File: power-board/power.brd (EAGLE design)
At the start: 100 x 80 mm, 2 parts, among them IC1 7805TV

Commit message: pow
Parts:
- added C1, C2, C3, C4: 100 nF, resistor:C025-025X050
- added D1: (no value), SparkFun-LED:LED5MM
- added R1: 470, resistor:0207/10
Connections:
- new net N$1: IC1.1, JP1.GND, R1.1
- new net N$2: D1.K, IC1.2, JP1.PWR
- new net N$3: D1.A, R1.2
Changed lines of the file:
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@@
 </element>
 <element name="IC1" library="linear" package="TO220V" value="7805TV" x="6.35" y="0"/>
+<element name="D1" library="SparkFun-LED" package="LED5MM" value="" x="3.81" y="-11.43"/>
+<element name="R1" library="resistor" package="0207/10" value="470" x="6.35" y="-19.05"/>
+<element name="C1" library="resistor" package="C025-025X050" value="100 nF" x="3.81" y="-24.13"/>
+<element name="C2" library="resistor" package="C025-025X050" value="100 nF" x="3.81" y="-31.75"/>
+<element name="C3" library="resistor" package="C025-025X050" value="100 nF" x="3.81" y="-39.37"/>
+<element name="C4" library="resistor" package="C025-025X050" value="100 nF" x="3.81" y="-46.99"/>
 </elements>
 <signals>
+<signal name="N$1">
+<contactref element="JP1" pad="GND"/>
+<contactref element="IC1" pad="1"/>
+<contactref element="R1" pad="1"/>
+<wire x1="3.81" y1="-2.54" x2="11.4554" y2="35.767" width="0" layer="19" extent="1-1"/>
+<wire x1="1.27" y1="-19.05" x2="3.81" y2="-2.54" width="0" layer="19" extent="1-1"/>
+</signal>
+<signal name="N$2">
+<contactref element="JP1" pad="PWR"/>
+<contactref element="IC1" pad="2"/>
+<contactref element="D1" pad="K"/>
+<wire x1="6.35" y1="-2.54" x2="11.43" y2="43.0878" width="0" layer="19" extent="1-1"/>
+<wire x1="5.08" y1="-11.43" x2="6.35" y2="-2.54" width="0" layer="19" extent="1-1"/>
+</signal>
+<signal name="N$3">
+<contactref element="R1" pad="2"/>
+<contactref element="D1" pad="A"/>
+<wire x1="2.54" y1="-11.43" x2="11.43" y2="-19.05" width="0" layer="19" extent="1-1"/>
+</signal>
 </signals>
 </board>

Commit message: power board ok
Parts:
- removed C3, C4: 100 nF, resistor:C025-025X050
- added ARDU: (no value), pinhead:1X03
- added DISPLAY, LED: (no value), pinhead:1X02
- added FOTOC: (no value), pinhead:1X04
- C2: value 100 nF -> 330 nF
- JP1: value POWER_JACKPTH_LOCK -> POWER_JACKPTH; device SparkFun-Connectors:POWER_JACK_PTH_LOCK -> SparkFun-Connectors:POWER_JACK_PTH
- R1: value 470 -> 680
- moved C1 55.9 mm to (3.81, 31.8), turned to 270 degrees
- moved C2 55.9 mm to (3.81, 24.1), turned to 270 degrees
- moved IC1 28.0 mm to (7.62, 27.9), turned to 90 degrees
- moved JP1 21.6 mm to (-5.08, 15.2), turned to 270 degrees
- moved D1 21.0 mm to (12.7, 7.62), turned to 270 degrees
- moved R1 20.3 mm to (6.35, 1.27)
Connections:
- removed net N$3: D1.A, R1.2
- new net N$5: ARDU.3, C1.2, C2.1, DISPLAY.2, FOTOC.3, FOTOC.4, IC1.2, JP1.GND, LED.2, R1.1
- new net N$6: C1.1, DISPLAY.1, IC1.3, LED.1
- net N$1: now also D1.K, R1.2; no longer IC1.1, JP1.GND, R1.1
- net N$2: now also ARDU.1, C2.2, D1.A, FOTOC.1, FOTOC.2, IC1.1; no longer D1.K, IC1.2
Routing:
- net N$5: track 0.00 -> 101.4 mm
- net N$2: track 0.00 -> 45.0 mm
- net N$6: track 0.00 -> 29.6 mm
- net N$3: track 0.00 -> 23.4 mm
- net N$1: track 0.00 -> 5.24 mm
- added copper zone on layer 16, net GND
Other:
- board size 100 x 80 mm -> 26.3 x 45.7 mm

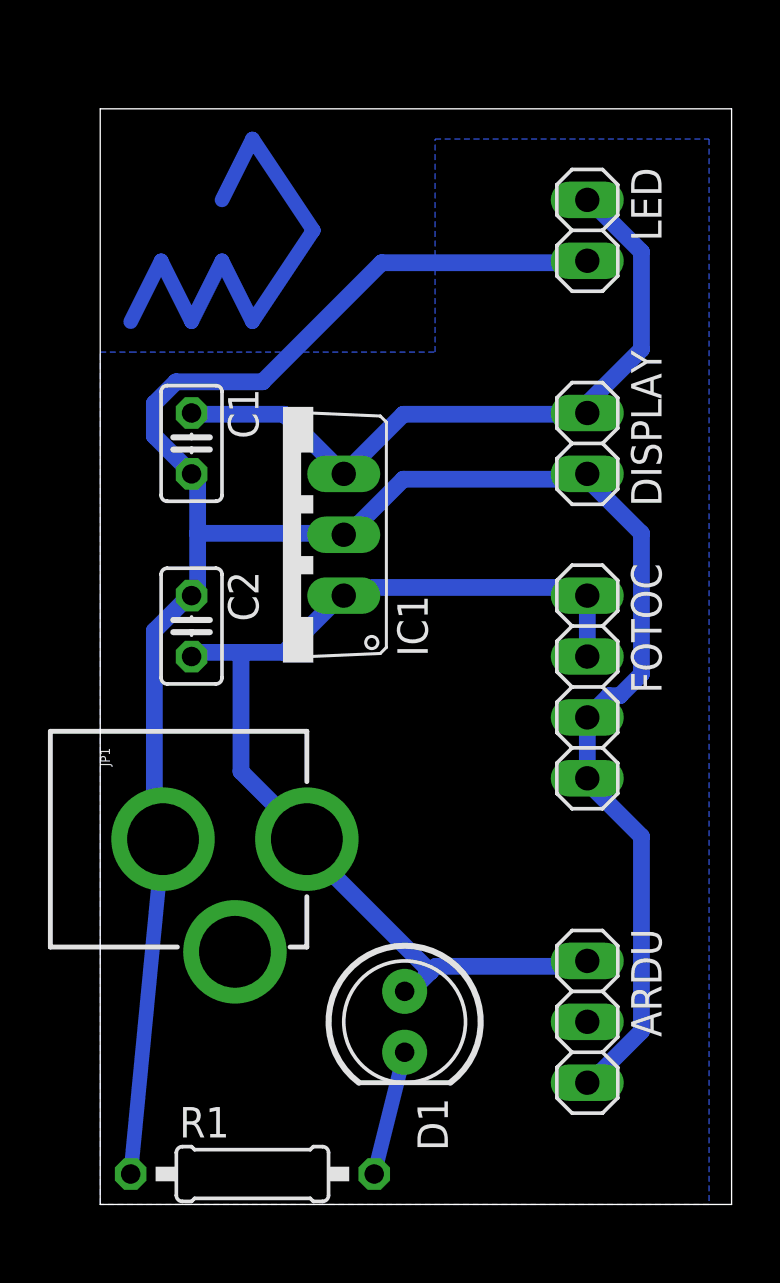
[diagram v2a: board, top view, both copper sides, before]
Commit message: Power board printed
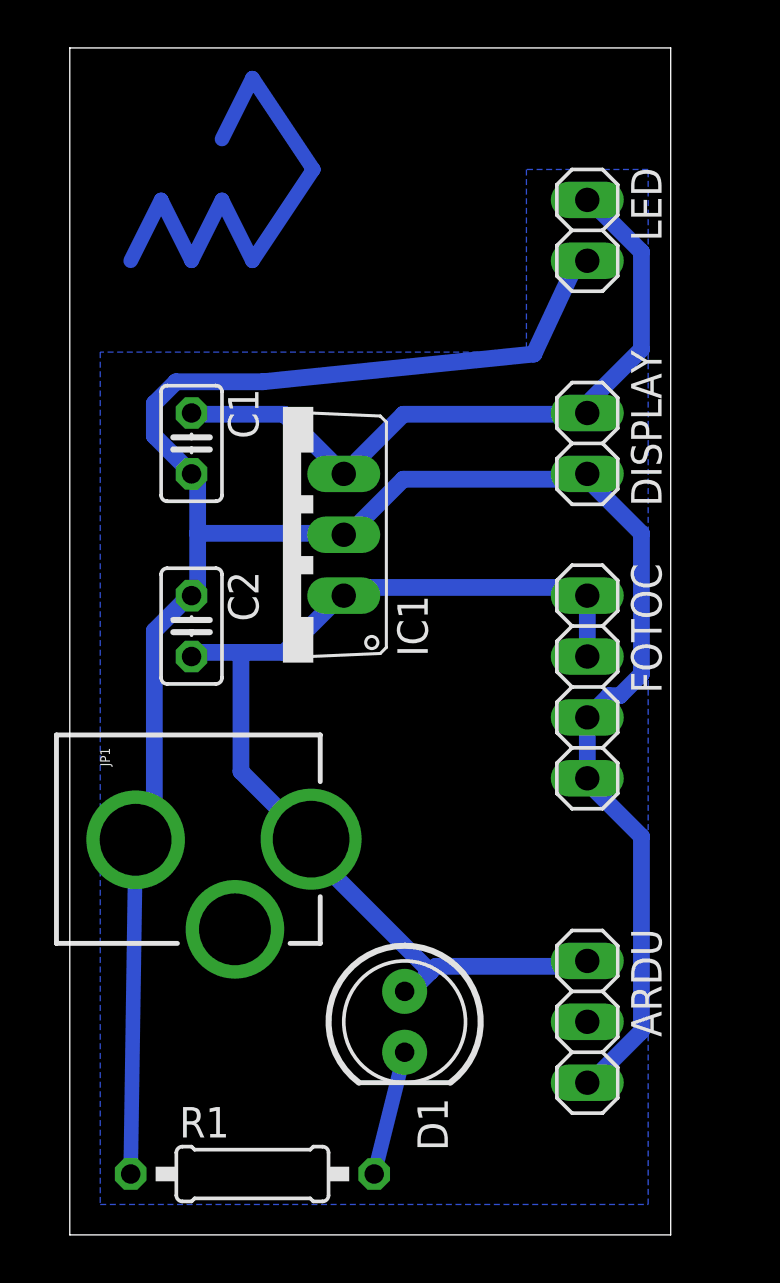
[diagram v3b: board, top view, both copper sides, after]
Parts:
- JP1: value POWER_JACKPTH -> POWER_JACKPTH_LOCK; device SparkFun-Connectors:POWER_JACK_PTH -> SparkFun-Connectors:POWER_JACK_PTH_LOCK
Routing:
- net N$5: track 101.4 -> 102.2 mm
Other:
- board size 26.3 x 45.7 mm -> 25.1 x 49.5 mm

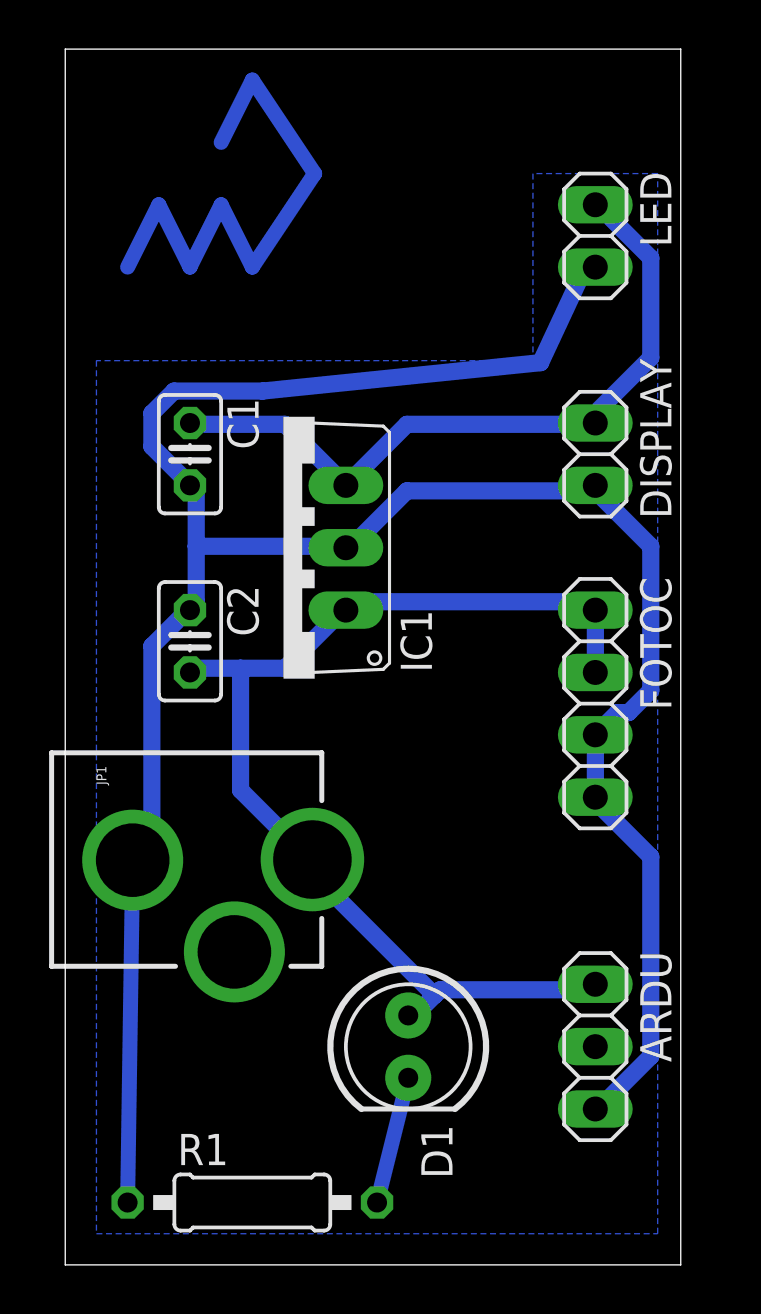
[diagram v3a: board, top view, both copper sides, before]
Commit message: Learned how to use net (instead of wires) cleaned connections in schematic made ground plane a real GND routed like a boss \m/
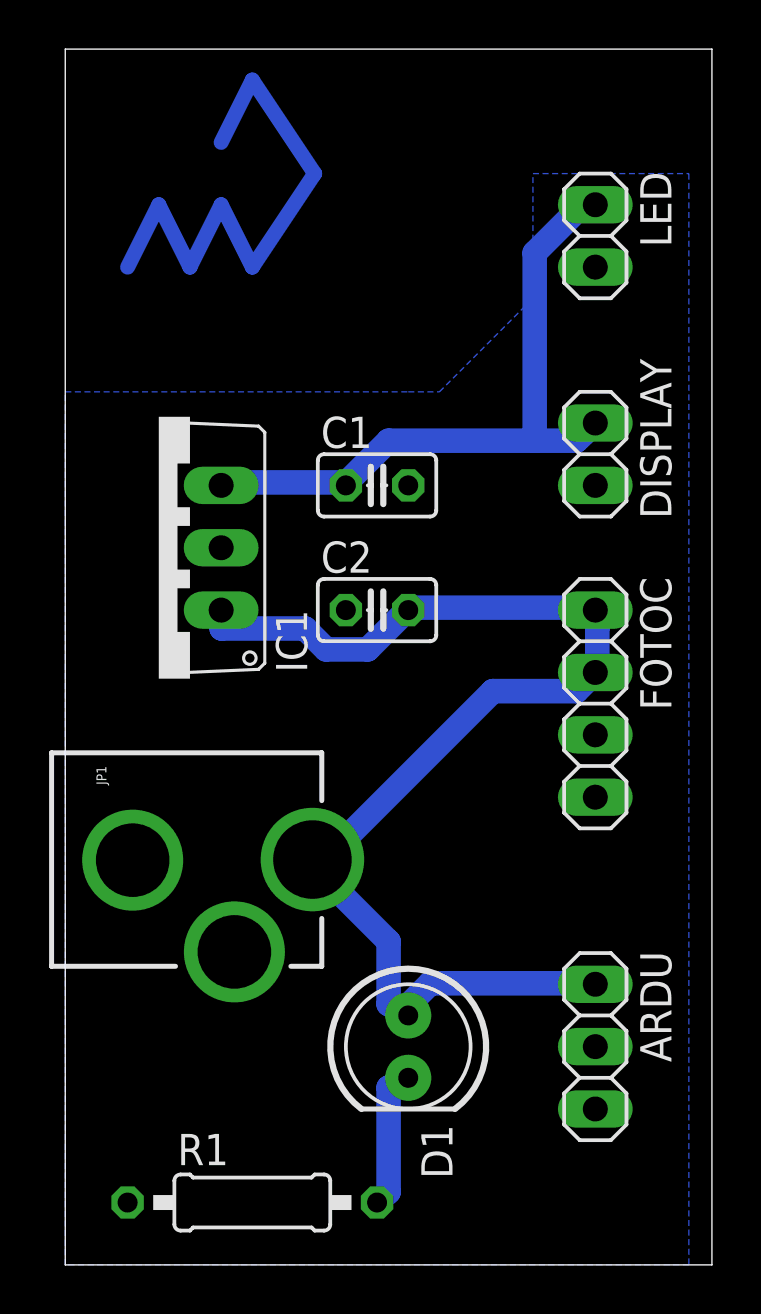
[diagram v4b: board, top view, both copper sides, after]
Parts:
- moved C1 7.73 mm to (11.4, 30.5), turned to 0 degrees
- moved C2 7.73 mm to (11.4, 25.4), turned to 0 degrees
- moved IC1 5.08 mm to (2.54, 27.9)
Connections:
- net N$2 renamed 12V
- net N$6 renamed 5V
- removed net N$5: ARDU.3, C1.2, C2.1, DISPLAY.2, FOTOC.3, FOTOC.4, IC1.2, JP1.GND, LED.2, R1.1
- new net GND: ARDU.3, C1.2, C2.1, DISPLAY.2, FOTOC.3, FOTOC.4, IC1.2, JP1.GND, JP1.GNDBREAK, LED.2, R1.1
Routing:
- net N$5: track 102.2 -> 0.00 mm
- net 12V: track 45.2 -> 50.8 mm
- net 5V: track 29.6 -> 27.3 mm
- net N$10: track 5.24 -> 5.78 mm
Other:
- board size 25.1 x 49.5 mm -> 26.3 x 49.5 mm
